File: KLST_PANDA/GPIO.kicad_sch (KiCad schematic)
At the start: 1 part, among them J15 GPIO

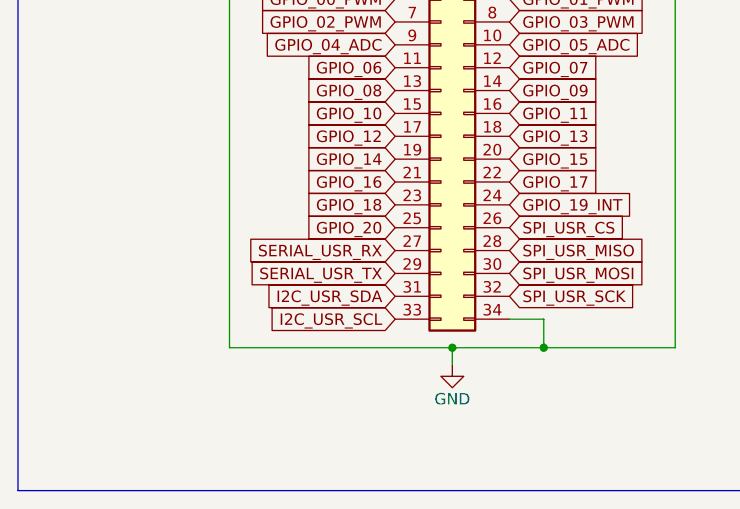
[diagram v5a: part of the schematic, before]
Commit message: changed `GPIO_20` to `GPIO_06` ( which was missing )
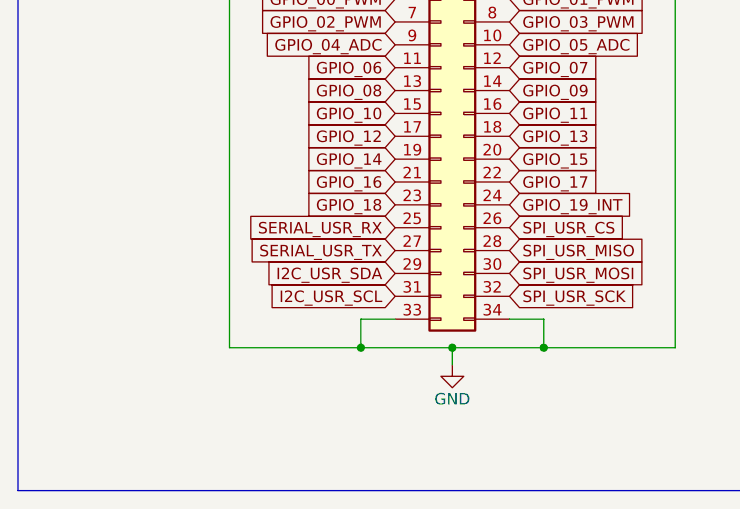
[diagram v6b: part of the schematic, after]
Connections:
- net GPIO_20 is gone; now on net SERIAL_USR_RX: J15.25 (Pin_25)
- net GND: now also J15.33 (Pin_33)
- net I2C_USR_SCL: now also J15.31 (Pin_31); no longer J15.33 (Pin_33)
- net I2C_USR_SDA: now also J15.29 (Pin_29); no longer J15.31 (Pin_31)
- net SERIAL_USR_RX: no longer J15.27 (Pin_27)
- net SERIAL_USR_TX: now also J15.27 (Pin_27); no longer J15.29 (Pin_29)
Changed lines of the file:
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@@
   (junction (at 63.5 78.105) (diameter 0) (color 0 0 0 0)
   )
+  (junction (at 53.34 78.105) (diameter 0) (color 0 0 0 0)
+  )
   (junction (at 73.66 78.105) (diameter 0) (color 0 0 0 0)
   )
@@
     (stroke (width 0) (type default))
   )
-  (wire (pts (xy 63.5 78.105) (xy 38.735 78.105))
+  (wire (pts (xy 53.34 78.105) (xy 38.735 78.105))
+    (stroke (width 0) (type default))
+  )
+  (wire (pts (xy 63.5 78.105) (xy 53.34 78.105))
     (stroke (width 0) (type default))
   )
@@
   )
   (wire (pts (xy 38.735 36.83) (xy 38.735 78.105))
+    (stroke (width 0) (type default))
+  )
+  (wire (pts (xy 53.34 74.93) (xy 53.34 78.105))
+    (stroke (width 0) (type default))
+  )
+  (wire (pts (xy 57.15 74.93) (xy 53.34 74.93))
     (stroke (width 0) (type default))
   )
@@
     )
   )
-  (global_label "I2C_USR_SCL" (shape input) (at 57.15 74.93 180) (fields_autoplaced)
-    (effects (font (size 1.27 1.27)) (justify right))
-    (property "Intersheetrefs" "${INTERSHEET_REFS}" (at 41.9071 74.93 0)
-      (effects (font (size 1.27 1.27)) (justify right) hide)
-    )
-  )
-  (global_label "SERIAL_USR_RX" (shape input) (at 57.15 67.31 180) (fields_autoplaced)
-    (effects (font (size 1.27 1.27)) (justify right))
-    (property "Intersheetrefs" "${INTERSHEET_REFS}" (at 39.6695 67.31 0)
+  (global_label "I2C_USR_SCL" (shape input) (at 57.15 72.39 180) (fields_autoplaced)
+    (effects (font (size 1.27 1.27)) (justify right))
+    (property "Intersheetrefs" "${INTERSHEET_REFS}" (at 41.9071 72.39 0)
+      (effects (font (size 1.27 1.27)) (justify right) hide)
+    )
+  )
+  (global_label "SERIAL_USR_RX" (shape input) (at 57.15 64.77 180) (fields_autoplaced)
+    (effects (font (size 1.27 1.27)) (justify right))
+    (property "Intersheetrefs" "${INTERSHEET_REFS}" (at 39.6695 64.77 0)
       (effects (font (size 1.27 1.27)) (justify right) hide)
     )
@@
     )
   )
-  (global_label "I2C_USR_SDA" (shape input) (at 57.15 72.39 180) (fields_autoplaced)
-    (effects (font (size 1.27 1.27)) (justify right))
-    (property "Intersheetrefs" "${INTERSHEET_REFS}" (at 41.8466 72.39 0)
-      (effects (font (size 1.27 1.27)) (justify right) hide)
-    )
-  )
-  (global_label "SERIAL_USR_TX" (shape input) (at 57.15 69.85 180) (fields_autoplaced)
-    (effects (font (size 1.27 1.27)) (justify right))
-    (property "Intersheetrefs" "${INTERSHEET_REFS}" (at 39.9719 69.85 0)
+  (global_label "I2C_USR_SDA" (shape input) (at 57.15 69.85 180) (fields_autoplaced)
+    (effects (font (size 1.27 1.27)) (justify right))
+    (property "Intersheetrefs" "${INTERSHEET_REFS}" (at 41.8466 69.85 0)
+      (effects (font (size 1.27 1.27)) (justify right) hide)
+    )
+  )
+  (global_label "SERIAL_USR_TX" (shape input) (at 57.15 67.31 180) (fields_autoplaced)
+    (effects (font (size 1.27 1.27)) (justify right))
+    (property "Intersheetrefs" "${INTERSHEET_REFS}" (at 39.9719 67.31 0)
       (effects (font (size 1.27 1.27)) (justify right) hide)
     )
@@
     )
   )
-  (global_label "GPIO_20" (shape input) (at 57.15 64.77 180) (fields_autoplaced)
-    (effects (font (size 1.27 1.27)) (justify right))
-    (property "Intersheetrefs" "${INTERSHEET_REFS}" (at 46.3823 64.77 0)
-      (effects (font (size 1.27 1.27)) (justify right) hide)
-    )
-  )

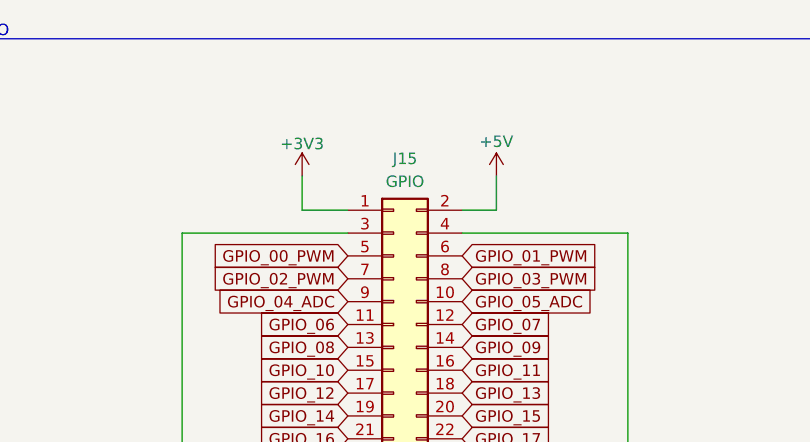
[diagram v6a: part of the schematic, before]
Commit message: added battery clip, updated to new KiCad version
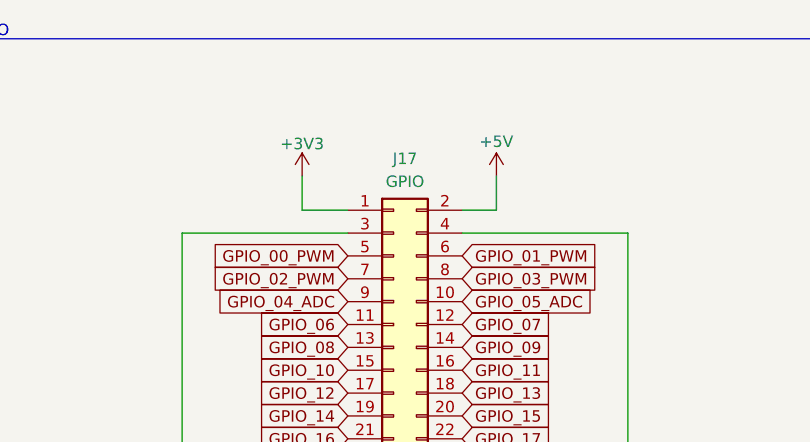
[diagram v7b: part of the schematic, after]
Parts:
- renumbered J15 to J17
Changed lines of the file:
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@@
   (symbol (lib_id "Connector_Generic:Conn_02x17_Odd_Even") (at 62.23 54.61 0) (unit 1)
     (in_bom yes) (on_board yes) (dnp no) (fields_autoplaced)
-    (property "Reference" "J15" (at 63.5 28.575 0)
+    (property "Reference" "J17" (at 63.5 28.575 0)
       (effects (font (size 1.27 1.27)))
     )
@@
       (project "KLST_PANDA"
         (path "/b4513875-4c57-4720-bcc5-43ead67fe18f/6bb3f144-c620-4528-bce8-cfaf92f97449"
-          (reference "J15") (unit 1)
+          (reference "J17") (unit 1)
         )
       )

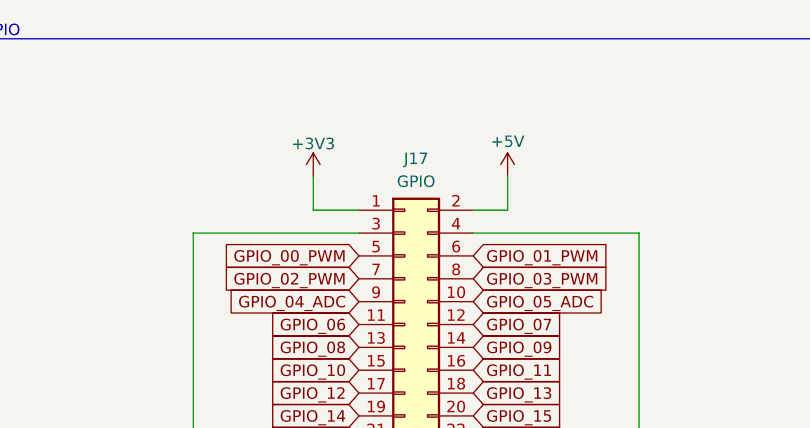
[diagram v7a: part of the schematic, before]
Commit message: removed DRC warnings and error, added power page
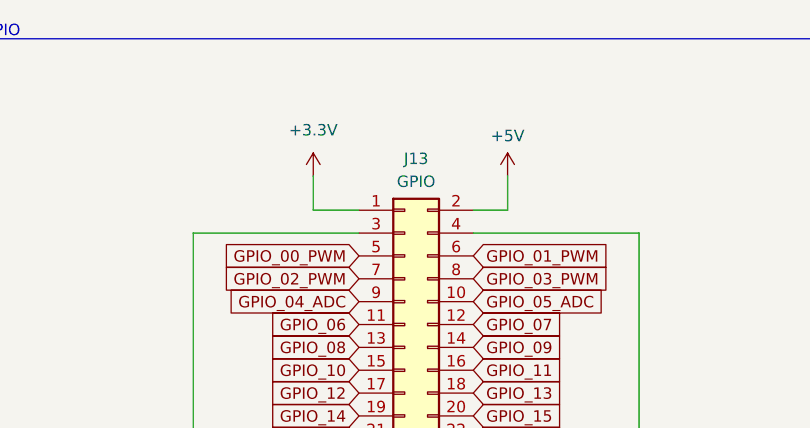
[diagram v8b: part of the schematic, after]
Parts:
- renumbered J17 to J13
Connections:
- net +3V3 renamed +3.3V
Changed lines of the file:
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@@
   (symbol (lib_id "Connector_Generic:Conn_02x17_Odd_Even") (at 62.23 54.61 0) (unit 1)
     (in_bom yes) (on_board yes) (dnp no) (fields_autoplaced)
-    (property "Reference" "J17" (at 63.5 28.575 0)
+    (property "Reference" "J13" (at 63.5 28.575 0)
       (effects (font (size 1.27 1.27)))
     )
@@
       (project "KLST_PANDA"
         (path "/b4513875-4c57-4720-bcc5-43ead67fe18f/6bb3f144-c620-4528-bce8-cfaf92f97449"
-          (reference "J17") (unit 1)
+          (reference "J13") (unit 1)
+        )
+      )
+    )
+  )
+  (symbol (lib_id "power:+3.3V") (at 52.07 30.48 0) (unit 1)
+    (in_bom yes) (on_board yes) (dnp no) (fields_autoplaced)
+    (property "Reference" "#PWR077" (at 52.07 34.29 0)
+      (effects (font (size 1.27 1.27)) hide)
+    )
+    (property "Value" "+3.3V" (at 52.07 25.4 0)
+      (effects (font (size 1.27 1.27)))
+    )
+    (property "Footprint" "" (at 52.07 30.48 0)
+      (effects (font (size 1.27 1.27)) hide)
+    )
+    (property "Datasheet" "" (at 52.07 30.48 0)
+      (effects (font (size 1.27 1.27)) hide)
+    )
+    (pin "1")
+    (instances
+      (project "KLST_PANDA"
+        (path "/b4513875-4c57-4720-bcc5-43ead67fe18f/47e8e77e-c64e-4c44-bfd8-2073580a3d85"
+          (reference "#PWR077") (unit 1)
+        )
+        (path "/b4513875-4c57-4720-bcc5-43ead67fe18f/6bb3f144-c620-4528-bce8-cfaf92f97449"
+          (reference "#PWR077") (unit 1)
         )
       )
@@
         )
         (path "/b4513875-4c57-4720-bcc5-43ead67fe18f/6bb3f144-c620-4528-bce8-cfaf92f97449"
-          (reference "#PWR087") (unit 1)
+          (reference "#PWR078") (unit 1)
         )
       )
     )
   )
-  (symbol (lib_id "power:+5V") (at 73.66 30.48 0) (unit 1)
-    (in_bom yes) (on_board yes) (dnp no)
-    (property "Reference" "#PWR0121" (at 73.66 34.29 0)
+  (symbol (lib_name "+5V_1") (lib_id "power:+5V") (at 73.66 30.48 0) (unit 1)
+    (in_bom yes) (on_board yes) (dnp no) (fields_autoplaced)
+    (property "Reference" "#PWR079" (at 73.66 34.29 0)
       (effects (font (size 1.27 1.27)) hide)
     )
-    (property "Value" "+5V" (at 73.66 26.67 0)
+    (property "Value" "+5V" (at 73.66 26.035 0)
       (effects (font (size 1.27 1.27)))
     )
@@
     (instances
       (project "KLST_PANDA"
-        (path "/b4513875-4c57-4720-bcc5-43ead67fe18f"
-          (reference "#PWR0121") (unit 1)
-        )
         (path "/b4513875-4c57-4720-bcc5-43ead67fe18f/6bb3f144-c620-4528-bce8-cfaf92f97449"
-          (reference "#PWR088") (unit 1)
+          (reference "#PWR079") (unit 1)
         )
       )
-    )
-  )
-  (symbol (lib_id "power:+3V3") (at 52.07 30.48 0) (unit 1)
-    (in_bom yes) (on_board yes) (dnp no)
-    (property "Reference" "#PWR0127" (at 52.07 34.29 0)
-      (effects (font (size 1.27 1.27)) hide)
-    )
-    (property "Value" "+3V3" (at 52.07 26.924 0)
-      (effects (font (size 1.27 1.27)))
-    )
-    (property "Footprint" "" (at 52.07 30.48 0)
-      (effects (font (size 1.27 1.27)) hide)
-    )
-    (property "Datasheet" "" (at 52.07 30.48 0)
-      (effects (font (size 1.27 1.27)) hide)
-    )
-    (pin "1")
-    (instances
-      (project "KLST_PANDA"
-        (path "/b4513875-4c57-4720-bcc5-43ead67fe18f"
-          (reference "#PWR0127") (unit 1)
-        )
-        (path "/b4513875-4c57-4720-bcc5-43ead67fe18f/6bb3f144-c620-4528-bce8-cfaf92f97449"
-          (reference "#PWR086") (unit 1)
-        )
-      )
